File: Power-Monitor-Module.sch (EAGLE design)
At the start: 17 parts, among them IC1 INA231, P1 2X5P, P2 2X5P, P3 1X4P

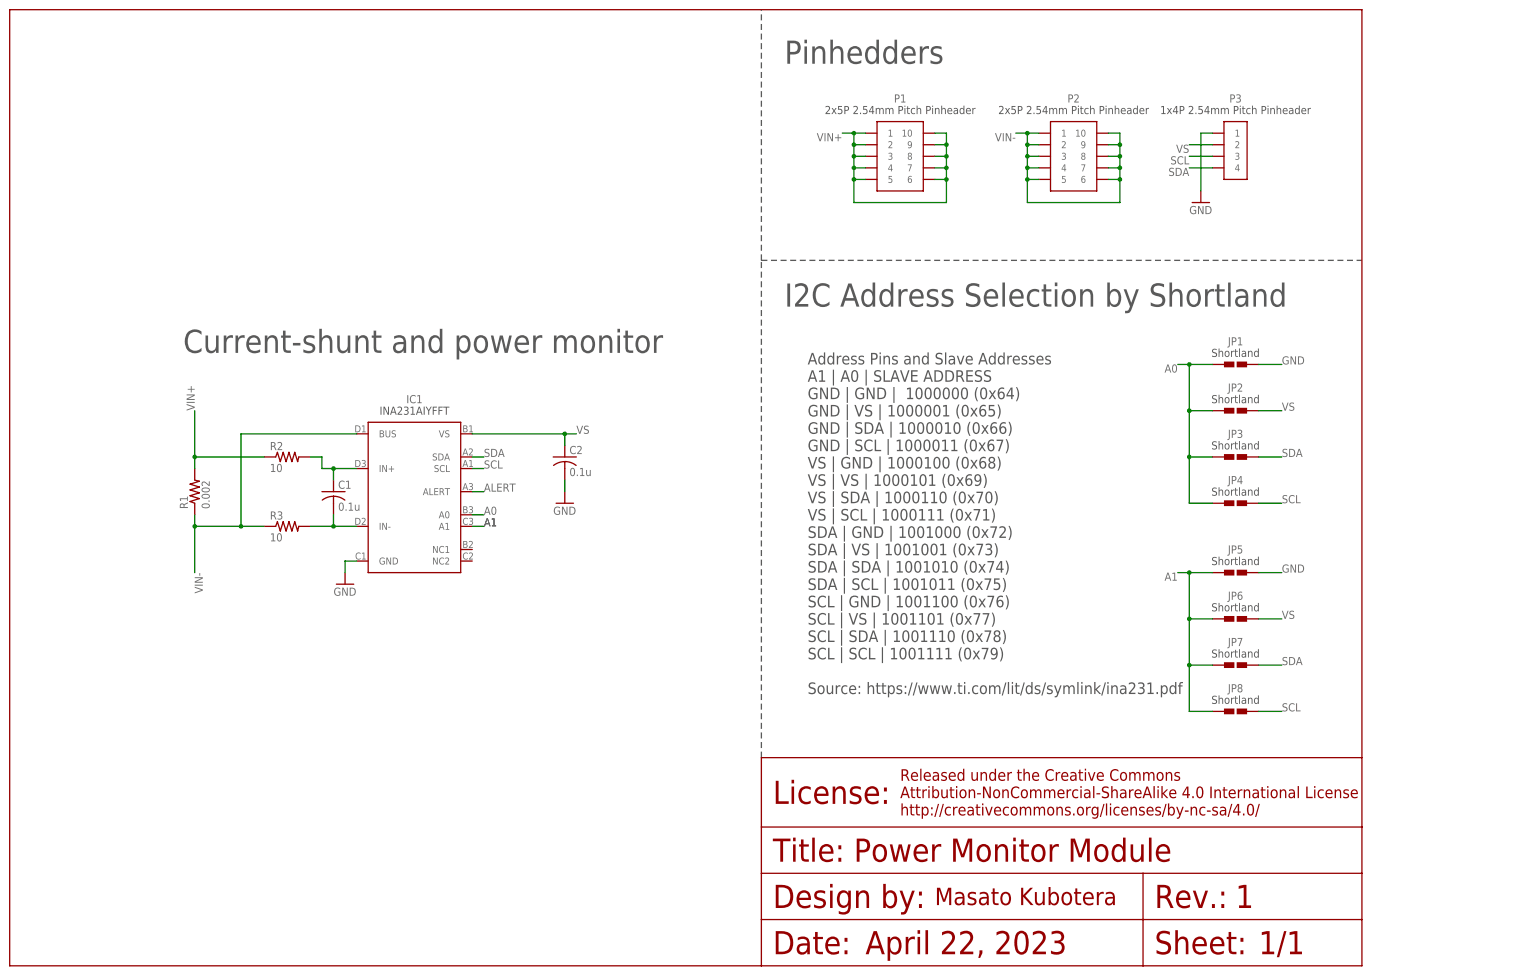
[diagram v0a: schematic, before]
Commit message: Made Rev.2 with the measurement IC changed to INA226.
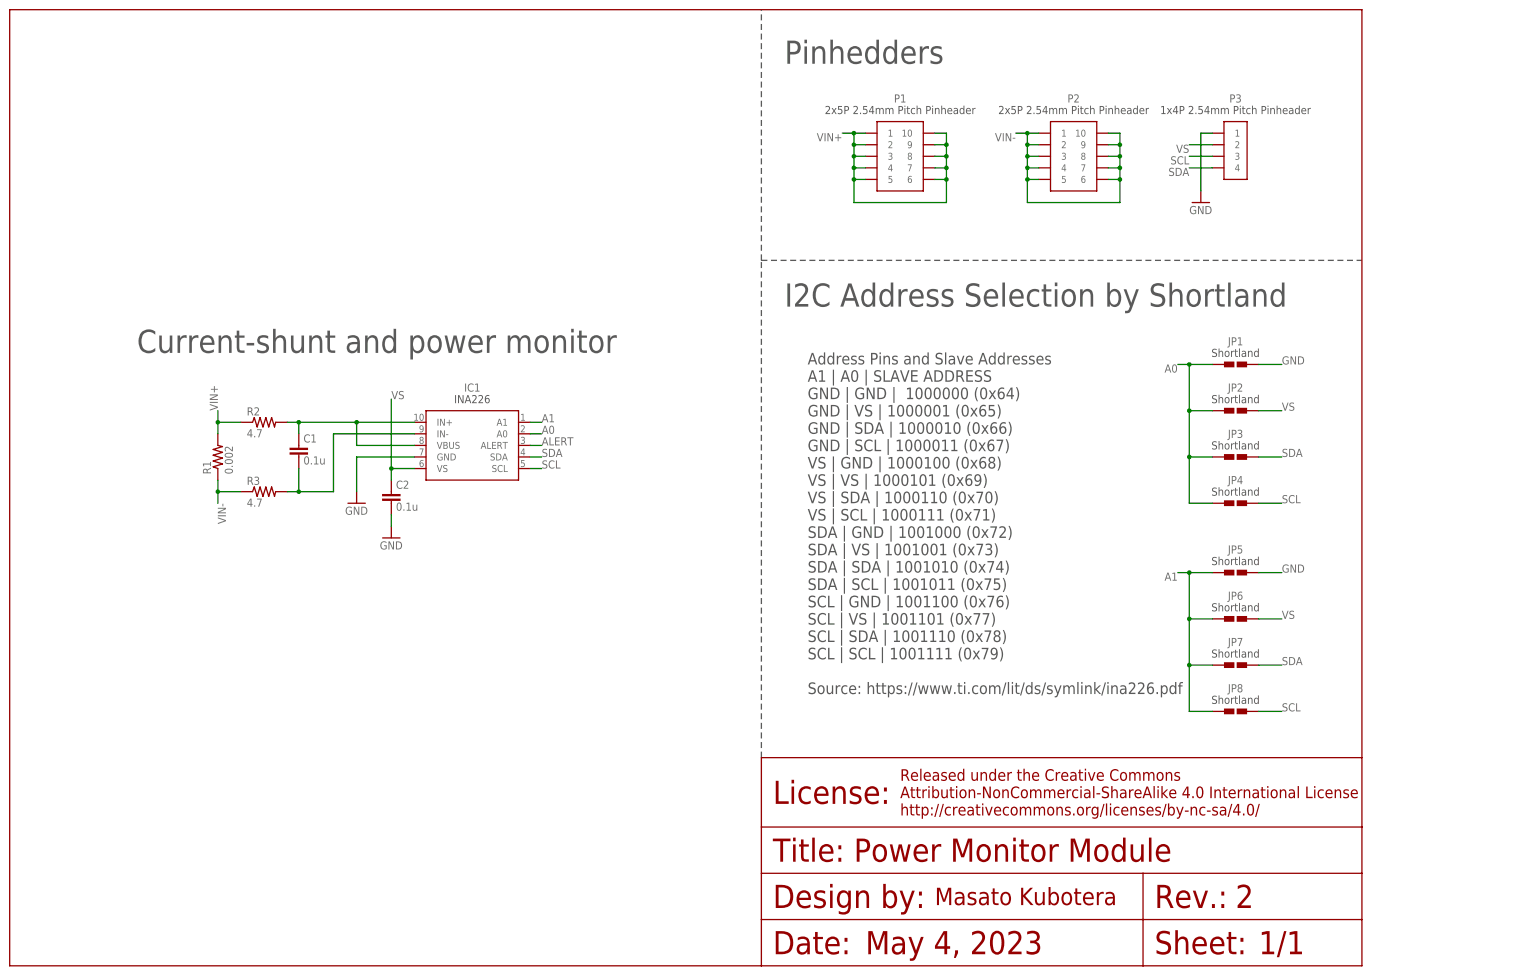
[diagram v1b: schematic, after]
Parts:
- C1, C2: device rcl:C-USC0603 -> rcl:C-EUC0402
- IC1: value INA231 -> INA226; device INA231:INA231 -> INA226:INA226
- R2, R3: value 10 -> 4.7; device rcl:R-US_R0603 -> rcl:R-US_R0402
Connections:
- net IN+: now also IC1.VBUS
- net VIN-: no longer IC1.BUS
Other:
- note added: "2"
- note added: "May 4, 2023"
- note removed: "1"
- note removed: "April 22, 2023"
- moved on the sheet: C1, C2, R1, R2, R3
